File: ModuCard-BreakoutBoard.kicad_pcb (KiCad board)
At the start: 4 copper layers, 85 x 97.7 mm, 55 parts, among them J1 09031967921, J10 USB_C_Receptacle_USB2.0_16P, J11 Barrel_Jack_Switch, J3 Conn_01x16_Pin, J4 Conn_01x16_Pin, J5 Conn_01x16_Pin, J6 Barrel_Jack_Switch, J7 Conn_01x02_Pin, J8 Conn_01x02_Pin, J9 RJ45_LED_Shielded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

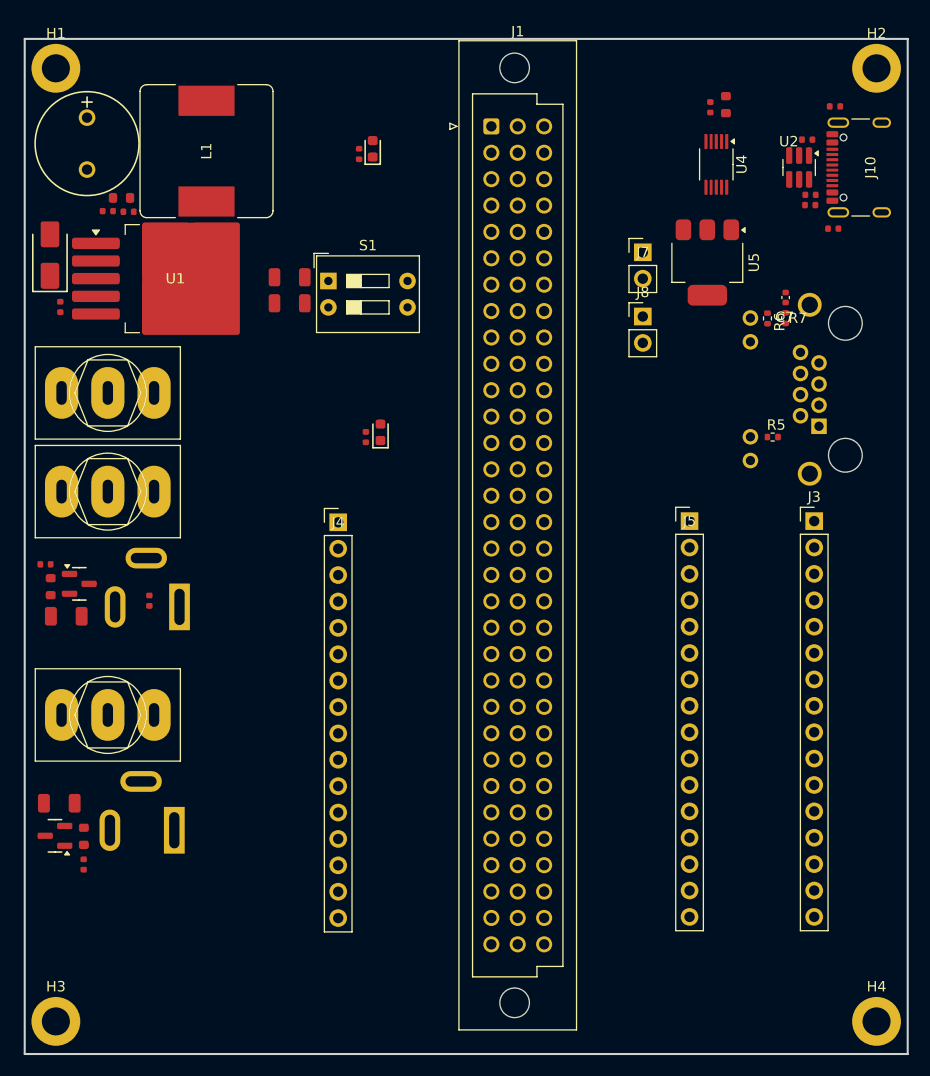
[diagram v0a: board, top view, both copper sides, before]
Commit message: Improve layout, add paths
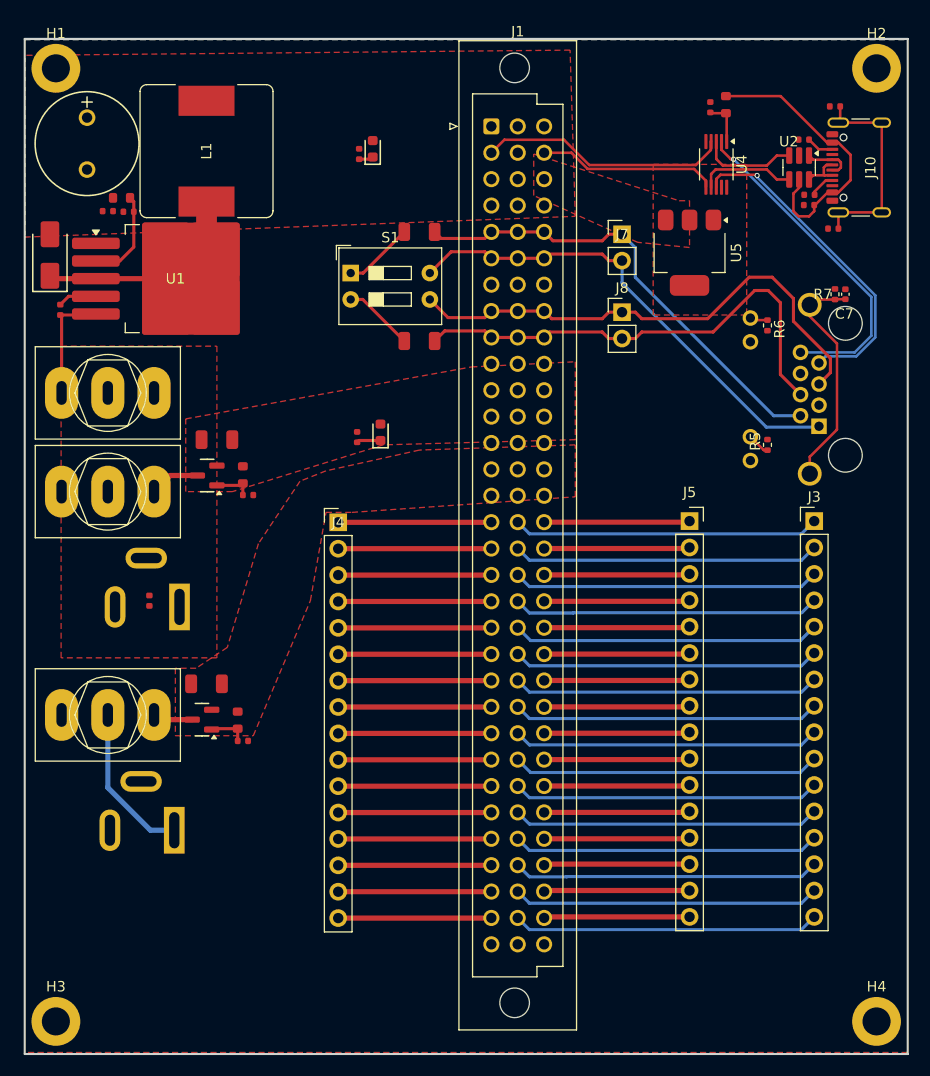
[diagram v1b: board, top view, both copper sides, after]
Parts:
- J5: footprint Connector_PinHeader_2.54mm:PinHeader_1x16_P2.54mm_Vertical -> Connector_PinSocket_2.54mm:PinSocket_1x16_P2.54mm_Vertical
- moved C2 22.3 mm to (108.5, 97.0), turned to 180 degrees
- moved R12 21.4 mm to (111.0, 100.4), turned to 90 degrees
- moved R11 20.6 mm to (111.5, 102.3), turned to 0 degrees
- moved R13 19.4 mm to (111.0, 126.0), turned to 0 degrees
- moved R14 18.6 mm to (110.5, 124.0)
- moved C6 18.3 mm to (107.5, 120.5)
- moved Q1 18.0 mm to (107.1, 124.0)
- moved Q2 16.1 mm to (107.6, 100.5), turned to 180 degrees
- moved R15 13.2 mm to (128.0, 77.0), turned to 0 degrees
- moved R16 13.0 mm to (128.0, 87.5), turned to 0 degrees
- moved C7 5.76 mm to (169.0, 83.0)
- moved R7 5.28 mm to (168.0, 83.0), turned to 90 degrees
- moved J7 2.65 mm to (147.5, 77.2)
- moved S1 2.28 mm to (121.4, 81.0)
- moved J8 2.04 mm to (147.5, 84.7)
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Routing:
- net /Connector/CAN2.+: track 0.00 -> 49.5 mm
- net /Connector/CAN1.-: track 0.00 -> 46.9 mm
- net /Connector/CAN2.-: track 0.00 -> 46.5 mm
- net /Connector/CAN1.+: track 0.00 -> 45.3 mm
- net /RJ45/USB_RJ.+: track 0.00 -> 32.3 mm, vias 0 -> 1
- net /RJ45/USB_RJ.-: track 0.00 -> 31.7 mm, vias 0 -> 1
- net /Connector/GPIOC4: track 0.00 -> 29.6 mm
- net /Connector/GPIOC9: track 0.00 -> 29.6 mm
- net /Connector/GPIOC8: track 0.00 -> 29.5 mm
- net /Connector/GPIOC3: track 0.00 -> 29.5 mm
- net /Connector/GPIOC1: track 0.00 -> 29.5 mm
- net /Connector/GPIOC6: track 0.00 -> 29.5 mm
- net /Connector/GPIOC13: track 0.00 -> 29.5 mm
- net /Connector/GPIOC12: track 0.00 -> 29.5 mm
- net /Connector/GPIOC11: track 0.00 -> 29.5 mm
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- added copper zone on F.Cu, net +12V
- added copper zone on F.Cu, net +12V_DC_JACK
- added copper zone on F.Cu, net +24V
- added copper zone on F.Cu, net +3V3
- added copper zone on F.Cu, net +5V standby
- added copper zone on B.Cu, net GND
- added copper zone on F.Cu, net GND

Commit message: Fix errors
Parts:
- added C5: 10n, Capacitor_SMD:C_0402_1005Metric, F.Cu at (168.5, 102.0)
- added R19: 33k, Resistor_SMD:R_0402_1005Metric, F.Cu at (169.5, 102.0)
- J11, J6: moved to F.Cu
- J5: footprint Connector_PinSocket_2.54mm:PinSocket_1x16_P2.54mm_Vertical -> Connector_PinHeader_2.54mm:PinHeader_1x16_P2.54mm_Vertical
- R15, R16: footprint PCM_JLCPCB:R_1206 -> PCM_JLCPCB:R_0603
- moved C3 5.02 mm to (107.0, 112.0), turned to 0 degrees
- moved R4 2.82 mm to (123.5, 72.0), turned to -90 degrees
- moved R3 2.30 mm to (123.5, 98.5), turned to -90 degrees
- moved R9 1.87 mm to (163.5, 67.0)
- moved C9 1.66 mm to (165.0, 76.0), turned to -90 degrees
- moved J6 1.63 mm to (103.7, 112.0)
- moved R11 0.84 mm to (111.0, 103.0), turned to -90 degrees
- moved D4 0.80 mm to (123.5, 96.0)
- moved R10 0.79 mm to (165.0, 74.0), turned to -90 degrees
- moved U5 0.71 mm to (154.5, 79.5)
- moved J11 0.60 mm to (104.4, 134.0)
- moved J9 0.35 mm to (166.5, 96.1)
- turned R15 to 180 degrees
- turned R16 to 180 degrees
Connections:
- R15 pad 1: Net-(R15-Pad1) -> /Connector/CAN1.+
- R15 pad 2: /Connector/CAN1.+ -> Net-(R15-Pad2)
- R16 pad 1: Net-(R16-Pad1) -> /Connector/CAN2.-
- R16 pad 2: /Connector/CAN2.- -> Net-(R16-Pad2)
- S1 pad 1: Net-(R15-Pad1) -> Net-(R15-Pad2)
- S1 pad 2: Net-(R16-Pad1) -> Net-(R16-Pad2)
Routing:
- net Net-(C5-Pad1): track 22.1 -> 7.97 mm
- net Net-(R16-Pad2): track 0.00 -> 7.46 mm
- net /RJ45/USB_RJ.+: track 32.3 -> 24.9 mm
- net Net-(R15-Pad2): track 0.00 -> 7.44 mm
- net Net-(R16-Pad1): track 6.82 -> 0.00 mm
- net Net-(R15-Pad1): track 6.80 -> 0.00 mm
- net /DIN41612_breakout/USB_DIN.-: track 17.3 -> 23.5 mm
- net /RJ45/USB_RJ.-: track 31.7 -> 25.7 mm
- net /USB/VBUS_IN: track 27.5 -> 22.1 mm
- net Net-(J10-CC2): track 2.63 -> 4.59 mm
- net Net-(SW2-B): track 15.1 -> 13.7 mm
- net /Connector/CAN2.+: track 49.5 -> 48.2 mm
- net Net-(D4-Pad1): track 2.32 -> 1.21 mm
- net Net-(J10-CC1): track 2.46 -> 3.35 mm
- net /Connector/CAN1.+: track 45.3 -> 45.9 mm
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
